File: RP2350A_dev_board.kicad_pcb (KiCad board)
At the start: 2 copper layers, 50 x 60 mm, 50 parts, among them J1 Debug Headers, J2 USB_C_Female_USB2.0_16P, J3 I2C Headers, SW1 Button, SW2 Bootstrap, U1 USBLC6-2SC6, U2 SPX3819M5-L-3-3, U3 RP2350A, U4 W25Q128JVS, Y2 12MHz Crystal GND2,4

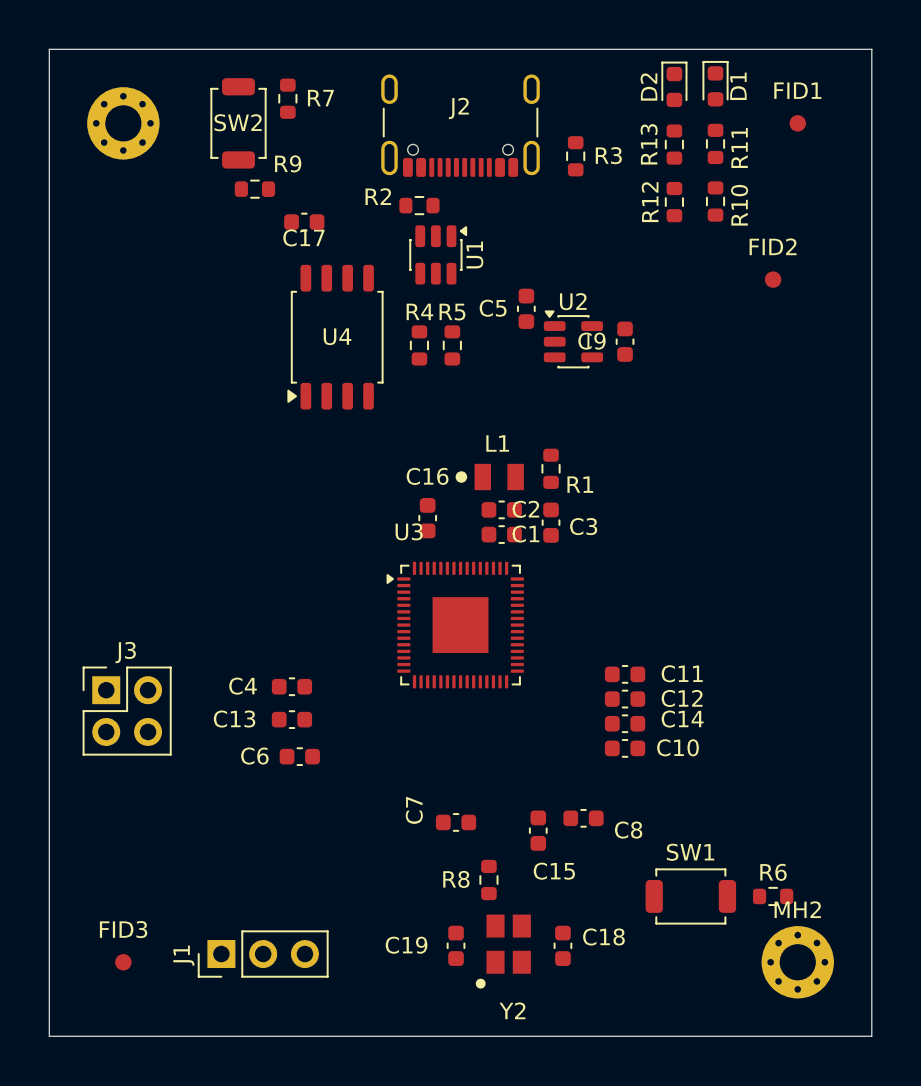
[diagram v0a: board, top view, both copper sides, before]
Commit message: Finished rough layout. Incorporated 5.1K pull-up resistors for I2C lines.
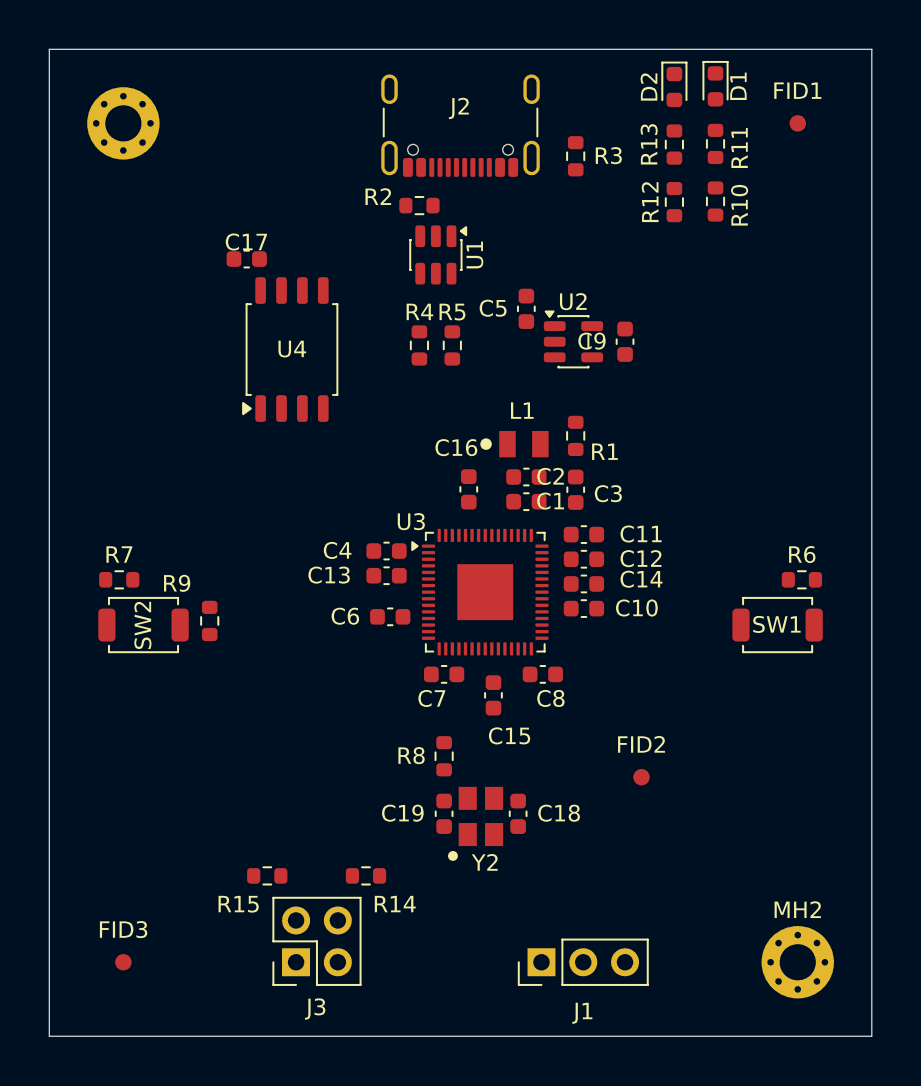
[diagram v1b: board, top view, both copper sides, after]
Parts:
- added R14: 5k1, Resistor_SMD:R_0603_1608Metric, F.Cu at (142.2, 121.2)
- added R15: 5k1, Resistor_SMD:R_0603_1608Metric, F.Cu at (136.2, 121.2)
- moved FID2 31.3 mm to (159.0, 115.2)
- moved SW2 31.0 mm to (128.7, 106.0), turned to 0 degrees
- moved R7 31.0 mm to (127.2, 103.2), turned to 180 degrees
- moved R9 26.4 mm to (132.8, 105.8), turned to -90 degrees
- moved J3 20.2 mm to (138.0, 126.5), turned to 90 degrees
- moved J1 19.5 mm to (152.9, 126.5)
- moved R6 19.3 mm to (168.8, 103.2), turned to 180 degrees
- moved SW1 17.3 mm to (167.3, 106.0)
- moved C13 10.5 mm to (143.5, 103.0)
- moved C6 10.1 mm to (143.7, 105.5)
- moved C4 10.1 mm to (143.5, 101.5)
- moved C8 9.09 mm to (153.0, 109.0)
- moved C7 9.03 mm to (147.0, 109.0)
- moved C10 8.86 mm to (155.5, 105.0)
- moved C11 8.86 mm to (155.5, 100.5)
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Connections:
- J3 pad 2: /I2C0_SCL -> /I2C0_SDA
- J3 pad 4: /I2C0_SDA -> /I2C0_SCL

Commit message: Modified PCB layout, added GND plane on layer 2, began adding GND vias.
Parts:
- moved R2 1.27 mm to (144.2, 80.2)
- moved U1 1.06 mm to (147.6, 83.4)
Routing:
- net (no net): vias 0 -> 39
- added copper zone on B.Cu, net GND

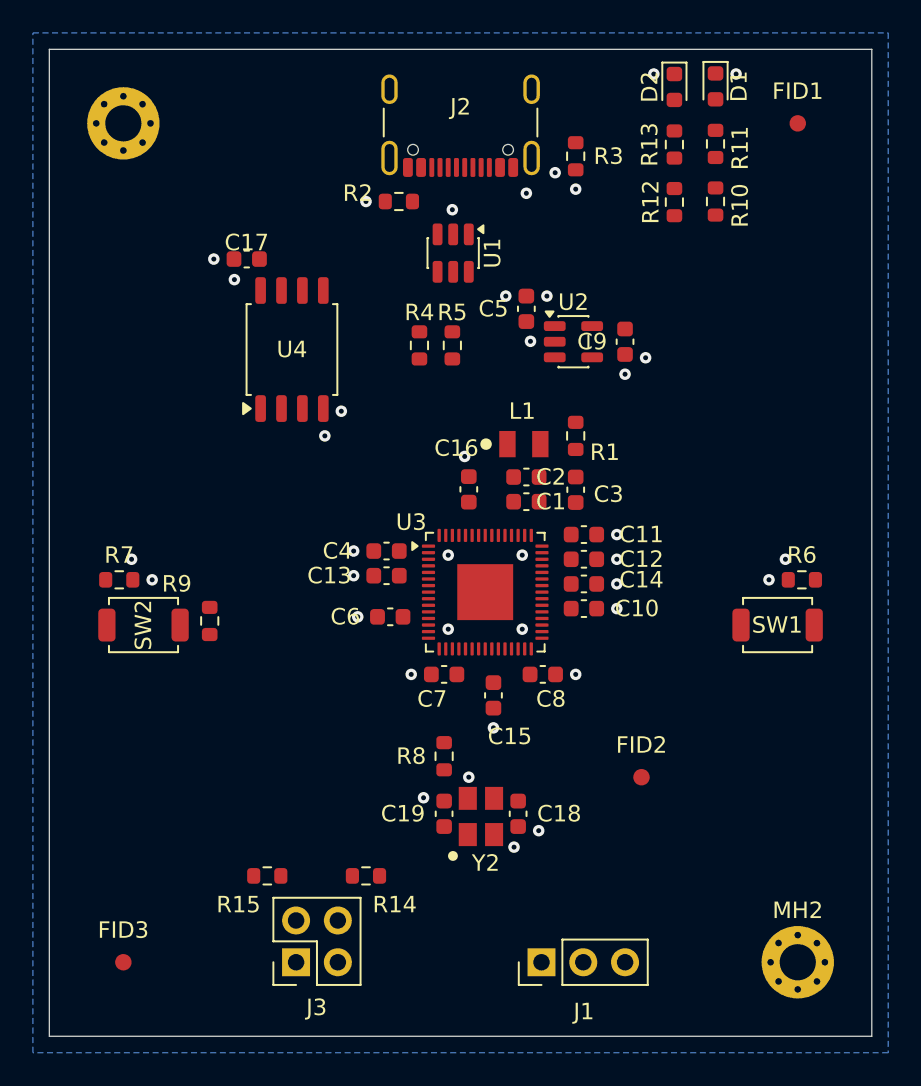
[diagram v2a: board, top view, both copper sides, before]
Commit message: Added vias to Voltage Regulator.
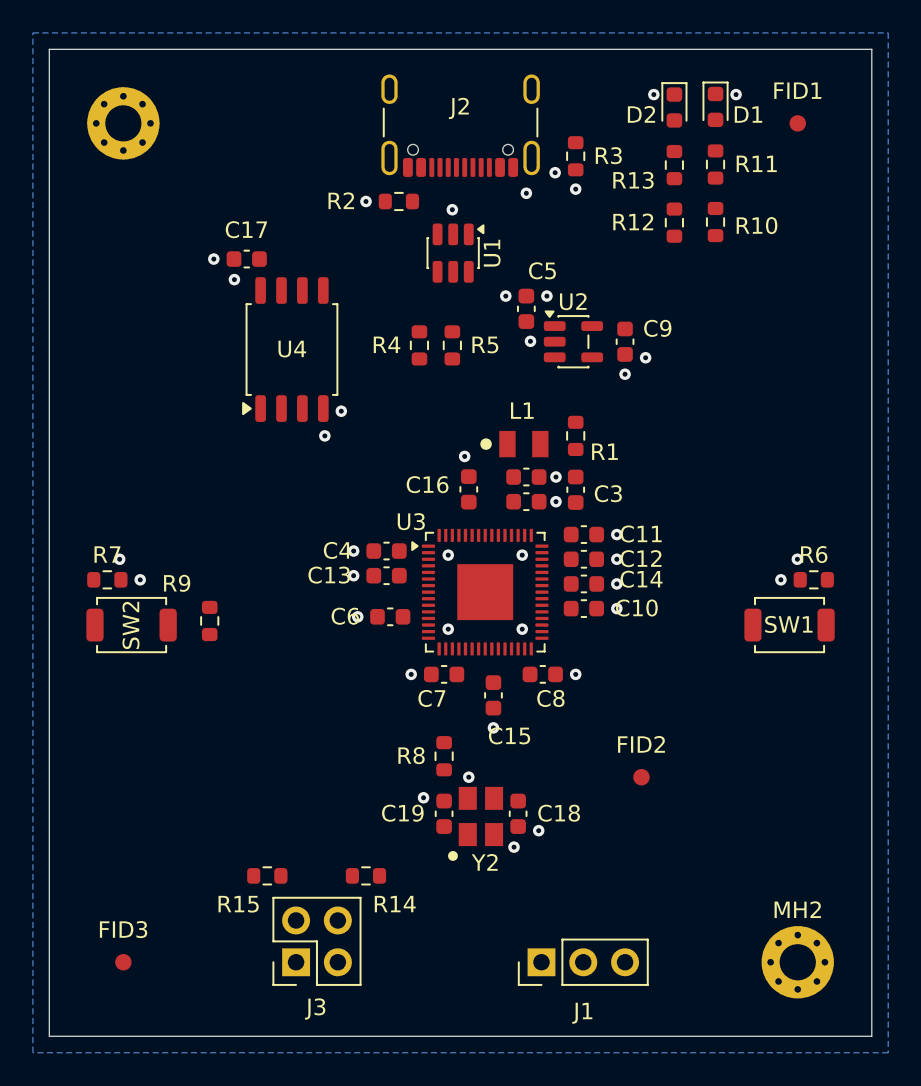
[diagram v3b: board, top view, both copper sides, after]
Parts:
- moved D1 1.25 mm to (163.5, 74.5)
- moved D2 1.25 mm to (161.0, 74.5)
- moved R10 1.25 mm to (163.5, 81.5)
- moved R11 1.25 mm to (163.5, 78.0)
- moved R12 1.25 mm to (161.0, 81.5)
- moved R13 1.25 mm to (161.0, 78.0)
- moved R6 0.72 mm to (169.5, 103.2)
- moved R7 0.72 mm to (126.5, 103.2)
- moved SW1 0.72 mm to (168.0, 106.0)
- moved SW2 0.72 mm to (128.0, 106.0)
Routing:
- net (no net): vias 39 -> 41
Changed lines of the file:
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@@
 	(footprint "Resistor_SMD:R_0603_1608Metric"
 		(layer "F.Cu")
-		(at 161 76.7875 90)
+		(at 161 78.0375 90)
 		(descr "Resistor SMD 0603 (1608 Metric), square (rectangular) end terminal, IPC-7351 nominal, (Body size source: IPC-SM-782 page 72, https://www.pcb-3d.com/wordpress/wp-content/uploads/ipc-sm-782a_amendment_1_and_2.pdf), generated with kicad-footprint-generator")
 		(tags "resistor")
 		(property "Reference" "R13"
-			(at 0 -1.5 90)
+			(at -0.9625 -2.5 180)
 			(layer "F.SilkS")
 			(effects
@@
 	(footprint "Button_Switch_SMD:SW_SPST_TS-1088-xR020"
 		(layer "F.Cu")
-		(at 167.275 106)
+		(at 168 106)
 		(descr "SMD Tactile Switch, 3.9x3x2 mm, https://lcsc.com/datasheet/lcsc_datasheet_2504101957_XUNPU-TS-1088-AR02016_C720477.pdf")
 		(tags "Tactile Switch")
@@
 	(footprint "LED_SMD:LED_0603_1608Metric"
 		(layer "F.Cu")
-		(at 161 73.2875 -90)
+		(at 161 74.5375 -90)
 		(descr "LED SMD 0603 (1608 Metric), square (rectangular) end terminal, IPC-7351 nominal, (Body size source: http://www.tortai-tech.com/upload/download/2011102023233369053.pdf), generated with kicad-footprint-generator")
 		(tags "LED")
 		(property "Reference" "D2"
-			(at 0 1.5 90)
+			(at 0.4625 2 180)
 			(layer "F.SilkS")
 			(effects
@@
 	(footprint "Resistor_SMD:R_0603_1608Metric"
 		(layer "F.Cu")
-		(at 161 80.2875 90)
+		(at 161 81.5375 90)
 		(descr "Resistor SMD 0603 (1608 Metric), square (rectangular) end terminal, IPC-7351 nominal, (Body size source: IPC-SM-782 page 72, https://www.pcb-3d.com/wordpress/wp-content/uploads/ipc-sm-782a_amendment_1_and_2.pdf), generated with kicad-footprint-generator")
 		(tags "resistor")
 		(property "Reference" "R12"
-			(at 0 -1.43 90)
+			(at 0 -2.5 180)
 			(layer "F.SilkS")
 			(effects
@@
 		(tags "resistor")
 		(property "Reference" "R2"
-			(at 2.5 0.5 0)
+			(at 3.5 0 0)
 			(layer "F.SilkS")
 			(effects
@@
 	(footprint "Resistor_SMD:R_0603_1608Metric"
 		(layer "F.Cu")
-		(at 163.5 76.75 90)
+		(at 163.5 78 90)
 		(descr "Resistor SMD 0603 (1608 Metric), square (rectangular) end terminal, IPC-7351 nominal, (Body size source: IPC-SM-782 page 72, https://www.pcb-3d.com/wordpress/wp-content/uploads/ipc-sm-782a_amendment_1_and_2.pdf), generated with kicad-footprint-generator")
 		(tags "resistor")
 		(property "Reference" "R11"
-			(at -0.25 1.5 90)
+			(at 0 2.5 180)
 			(layer "F.SilkS")
 			(effects
@@
 		(tags "resistor")
 		(property "Reference" "R5"
-			(at 2 0 180)
+			(at 0 2 180)
 			(layer "F.SilkS")
 			(effects
@@
 		(tags "capacitor")
 		(property "Reference" "C16"
-			(at -2.5 0.75 180)
+			(at -0.25 2.5 180)
 			(layer "F.SilkS")
 			(effects
@@
 	(footprint "Resistor_SMD:R_0603_1608Metric"
 		(layer "F.Cu")
-		(at 168.75 103.25 180)
+		(at 169.475 103.25 180)
 		(descr "Resistor SMD 0603 (1608 Metric), square (rectangular) end terminal, IPC-7351 nominal, (Body size source: IPC-SM-782 page 72, https://www.pcb-3d.com/wordpress/wp-content/uploads/ipc-sm-782a_amendment_1_and_2.pdf), generated with kicad-footprint-generator")
 		(tags "resistor")
@@
 	(footprint "Resistor_SMD:R_0603_1608Metric"
 		(layer "F.Cu")
-		(at 163.5 80.25 90)
+		(at 163.5 81.5 90)
 		(descr "Resistor SMD 0603 (1608 Metric), square (rectangular) end terminal, IPC-7351 nominal, (Body size source: IPC-SM-782 page 72, https://www.pcb-3d.com/wordpress/wp-content/uploads/ipc-sm-782a_amendment_1_and_2.pdf), generated with kicad-footprint-generator")
 		(tags "resistor")
 		(property "Reference" "R10"
-			(at -0.25 1.5 90)
+			(at -0.25 2.5 180)
 			(layer "F.SilkS")
 			(effects
@@
 		(tags "resistor")
 		(property "Reference" "R4"
-			(at 2 0 180)
+			(at 0 -2 180)
 			(layer "F.SilkS")
 			(effects
@@
 			(at 1.5 0 0)
 			(layer "F.SilkS")
+			(hide yes)
 			(effects
 				(font
@@
 			(at -1.5 0 0)
 			(layer "F.SilkS")
+			(hide yes)
 			(effects
 				(font
@@
 		(tags "capacitor")
 		(property "Reference" "C17"
-			(at 0 1 0)
+			(at 0 1.75 0)
 			(layer "F.SilkS")
 			(effects
@@
 		(tags "capacitor")
 		(property "Reference" "C5"
-			(at 0 -2 180)
+			(at 2.275 1 180)
 			(layer "F.SilkS")
 			(effects
@@
 	(footprint "Button_Switch_SMD:SW_SPST_TS-1088-xR020"
 		(layer "F.Cu")
-		(at 128.725 106)
+		(at 128 106)
 		(descr "SMD Tactile Switch, 3.9x3x2 mm, https://lcsc.com/datasheet/lcsc_datasheet_2504101957_XUNPU-TS-1088-AR02016_C720477.pdf")
 		(tags "Tactile Switch")
@@
 	(footprint "LED_SMD:LED_0603_1608Metric"
 		(layer "F.Cu")
-		(at 163.5 73.25 -90)
+		(at 163.5 74.5 -90)
 		(descr "LED SMD 0603 (1608 Metric), square (rectangular) end terminal, IPC-7351 nominal, (Body size source: http://www.tortai-tech.com/upload/download/2011102023233369053.pdf), generated with kicad-footprint-generator")
 		(tags "LED")
 		(property "Reference" "D1"
-			(at 0 -1.43 90)
+			(at 0.5 -2 180)
 			(layer "F.SilkS")
 			(effects
@@
 	(footprint "Resistor_SMD:R_0603_1608Metric"
 		(layer "F.Cu")
-		(at 127.25 103.25 180)
+		(at 126.525 103.25 180)
 		(descr "Resistor SMD 0603 (1608 Metric), square (rectangular) end terminal, IPC-7351 nominal, (Body size source: IPC-SM-782 page 72, https://www.pcb-3d.com/wordpress/wp-content/uploads/ipc-sm-782a_amendment_1_and_2.pdf), generated with kicad-footprint-generator")
 		(tags "resistor")
@@
 		(tags "capacitor")
 		(property "Reference" "C9"
-			(at 0 2 0)
+			(at -0.775 -2 0)
 			(layer "F.SilkS")
 			(effects
@@
 	)
 	(via
-		(at 128 102)
+		(at 127.275 102)
 		(size 0.7)
 		(drill 0.3)
@@
 	)
 	(via
-		(at 129.25 103.25)
+		(at 128.525 103.25)
 		(size 0.7)
 		(drill 0.3)
@@
 	)
 	(via
-		(at 167.75 102)
+		(at 168.475 102)
 		(size 0.7)
 		(drill 0.3)
@@
 	)
 	(via
+		(at 153.8 98.5)
+		(size 0.7)
+		(drill 0.3)
+		(layers "F.Cu" "B.Cu")
+		(net 0)
+	)
+	(via
 		(at 150.75 86)
 		(size 0.7)
@@
 	)
 	(via
-		(at 166.75 103.25)
+		(at 167.475 103.25)
 		(size 0.7)
 		(drill 0.3)
@@
 	)
 	(via
-		(at 159.75 72.5)
+		(at 159.75 73.75)
 		(size 0.7)
 		(drill 0.3)
@@
 	)
 	(via
-		(at 164.75 72.5)
+		(at 164.75 73.75)
+		(size 0.7)
+		(drill 0.3)
+		(layers "F.Cu" "B.Cu")
+		(net 0)
+	)
+	(via
+		(at 153.8 97)
 		(size 0.7)
 		(drill 0.3)

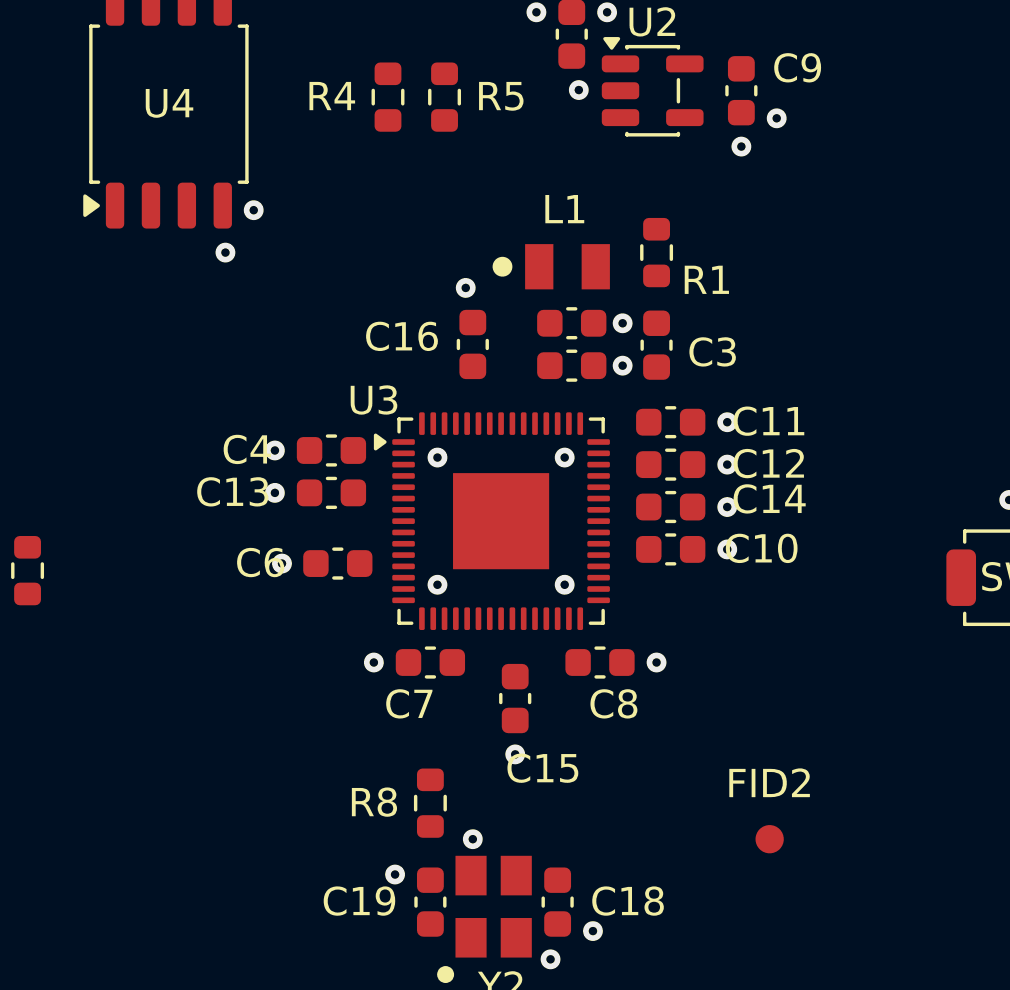
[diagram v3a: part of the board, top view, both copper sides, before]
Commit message: Fixed via and ground plane interractions. Added +1V1 and +3V3 planes.
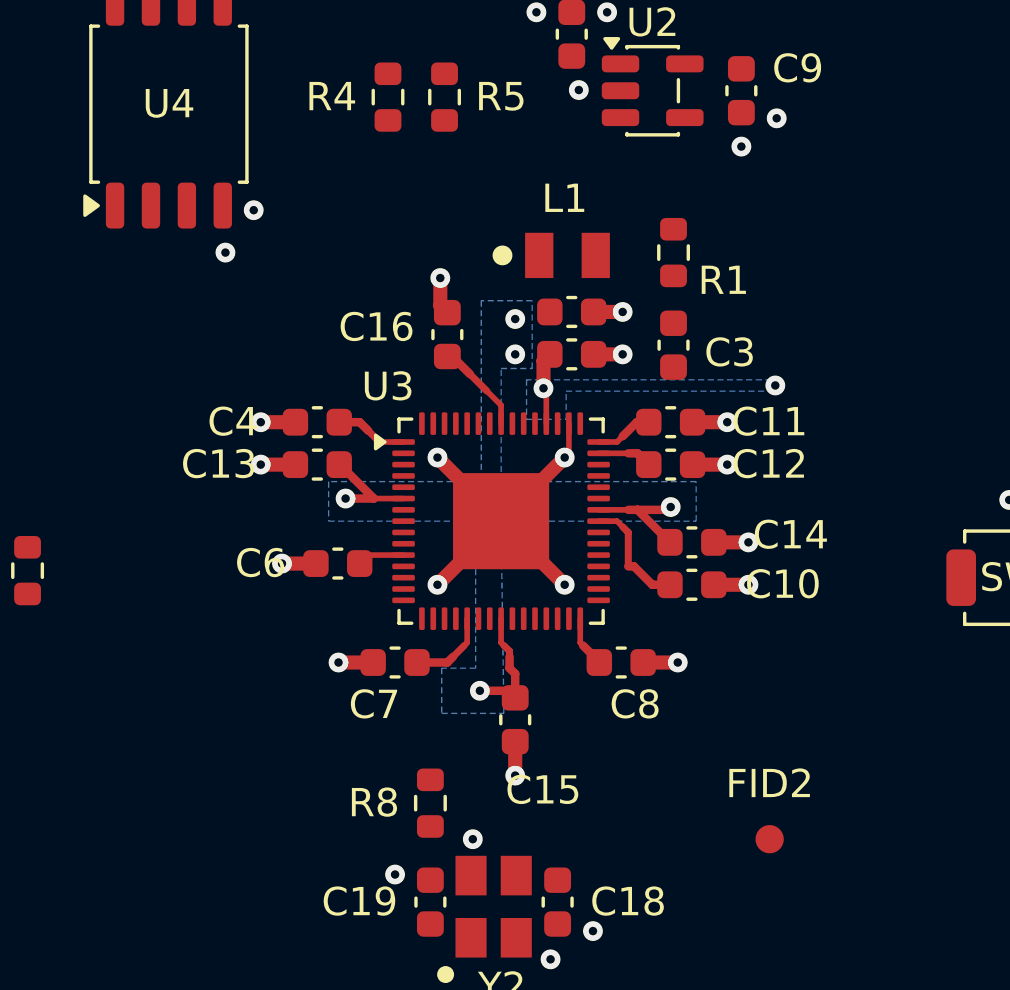
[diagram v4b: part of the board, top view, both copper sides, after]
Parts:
- moved C10 1.46 mm to (156.2, 106.2)
- moved C14 1.46 mm to (156.2, 104.8)
- moved C7 1.25 mm to (145.8, 109.0)
- moved C13 1.12 mm to (143.0, 102.0)
- moved C4 1.12 mm to (143.0, 100.5)
- moved C16 0.97 mm to (147.6, 97.4)
- moved C15 0.75 mm to (150.0, 111.0)
- moved C8 0.75 mm to (153.8, 109.0)
- moved C3 0.60 mm to (155.6, 97.8)
- moved R1 0.60 mm to (155.6, 94.5)
- moved C1 0.40 mm to (152.0, 98.1)
- moved C2 0.40 mm to (152.0, 96.6)
- moved L1 0.40 mm to (152.8, 94.6)
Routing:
- net GND: track 0.00 -> 29.6 mm, vias 0 -> 41
- net +3V3: track 0.00 -> 23.0 mm, vias 0 -> 2
- net +1V1: track 0.00 -> 12.4 mm, vias 0 -> 5
- net (no net): vias 41 -> 0
- added copper zone on B.Cu, net +1V1
- added copper zone on B.Cu, net +3V3
